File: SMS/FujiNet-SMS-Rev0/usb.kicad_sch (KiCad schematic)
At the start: 15 parts, among them J4 USB-C, U10 CP2102N-A02-GQFN28, U11 UMH3N

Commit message: SMS Rev0 v2: co-designed floorplan, region sheets, E9 pull-downs, frozen refs and nets
Floorplan study (docs/floorplan-study.md): the SMS edge is the JEDEC
32-pin memory pinout unrolled, so SRAM0 standing upright in the ROM spot
takes A0-A12 / D0-D7 / GND with no crossing.  gen_pcb.sram0_fanin draws
that fan-in locked (funnel, two corner wraps, B-finger jog vias, escape
vias for CE# and OE#).  Four candidates scored and trial-routed in
parallel; P3 (RP2354B straight north of SRAM0, SRAM1 west, glue east over
the strobes) routes best (45 unrouted after 4 passes vs 50 for the first
layout) and reads straight across on the schematic page.

- placement.py: candidates as blocks; the RP2354B + ring as a rigid macro
  (turns as a whole, dvdd_island turns with it); per-variant In4 +5V
  island polygon; label area for the shell
- design.py: sheets are board regions (cart-bus, rp-core, fujinet, usb,
  power); the RP2354B as a two-unit symbol (GPIO on cart-bus, core on
  rp-core); resistor packs one unit per resistor; RP2350-E9 4.7k
  pull-downs on GAME/LOAD/RAM_WE/MBOX/SA19 (check_nets asserts <= 8.2k);
  bring-up pads (CE, OE, WE, PWR_OK, rails, DVDD)
- geographic references (tools/annotate.py -> tools/refs.lock); net names
  frozen in tools/nets.lock (gen_sch fails if a redraw changes one)
- sch_draft.py: an every-pin-labelled draft of the final hierarchy so the
  board is built while the sheets are drawn; sch_draw lint for wired
  sheets (one piece per net, no 4-way junctions, wires clear of text,
  crossing count); sch_place.py mirror check
- check_parts_inside: footprint keep-outs (the S3 antenna bars parts)
- shell: RESET plunger redesigned (captive flange under the guide, stem
  on the TS-1187A actuator, travel asserts, interference part)

ERC 0, parity 126/126, check_nets 442/442, check_glue 8192/8192.
Board placed, not routed yet.

Co-Authored-By: Claude Opus 5.5 <noreply@anthropic.com>
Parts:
- removed C34: 1uF, FujiNet-SMS:C_0603_1608Metric, symbol Device:C
- removed C35, C36: 100nF, FujiNet-SMS:C_0603_1608Metric, symbol Device:C
- removed C37: 4.7uF, FujiNet-SMS:C_0603_1608Metric, symbol Device:C
- removed D5, D6: ESD5Z5.0T1G, FujiNet-SMS:D_SOD-523, symbol Diode:ESD5Zxx
- removed J4: USB-C, FujiNet-SMS:USB_C_Receptacle_HRO_TYPE-C-31-M-12, symbol Connector:USB_C_Receptacle_USB2.0_16P
- removed R17, R18: 5.1k, FujiNet-SMS:R_0603_1608Metric, symbol Device:R
- removed R19: 22k, FujiNet-SMS:R_0603_1608Metric, symbol Device:R
- removed R20: 47k, FujiNet-SMS:R_0603_1608Metric, symbol Device:R
- removed R21: 10k, FujiNet-SMS:R_0603_1608Metric, symbol Device:R
- removed U10: CP2102N-A02-GQFN28, FujiNet-SMS:QFN-28-1EP_5x5mm_P0.5mm_EP3.35x3.35mm, symbol Interface_USB:CP2102N-Axx-xQFN28
- removed U11: UMH3N, FujiNet-SMS:SOT-363_SC-70-6, symbol Transistor_BJT:UMH3N
- added C13, C5: 100nF, FujiNet-SMS:C_0603_1608Metric, symbol Device:C
- added C14: 4.7uF, FujiNet-SMS:C_0603_1608Metric, symbol Device:C
- added C4: 1uF, FujiNet-SMS:C_0603_1608Metric, symbol Device:C
- added D2, D3: ESD5Z5.0T1G, FujiNet-SMS:D_SOD-523, symbol Diode:ESD5Zxx
- added J2: USB-C, FujiNet-SMS:USB_C_Receptacle_HRO_TYPE-C-31-M-12, symbol Connector:USB_C_Receptacle_USB2.0_16P
- added R1, R2: 5.1k, FujiNet-SMS:R_0603_1608Metric, symbol Device:R
- added R12: 22k, FujiNet-SMS:R_0603_1608Metric, symbol Device:R
- added R13: 47k, FujiNet-SMS:R_0603_1608Metric, symbol Device:R
- added R9: 10k, FujiNet-SMS:R_0603_1608Metric, symbol Device:R
- added U2: CP2102N-A02-GQFN28, FujiNet-SMS:QFN-28-1EP_5x5mm_P0.5mm_EP3.35x3.35mm, symbol Interface_USB:CP2102N-Axx-xQFN28
- added U3: UMH3N, FujiNet-SMS:SOT-363_SC-70-6, symbol Transistor_BJT:UMH3N
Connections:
- net +3V3: now also C13.1, C14.1, R9.1, U2.6 (VDD), U2.7 (VREGIN)
- net CC1: now also J2.A5 (CC1), R1.1
- net CC2: now also J2.B5 (CC2), R2.1
- net CP_RST: now also R9.2, U2.9 (~{RST})
- net GND: now also C13.2, C14.2, C4.2, C5.2, D2.2 (A), D3.2 (A), J2.A1 (GND), J2.A12 (GND), J2.B1 (GND), J2.B12 (GND), J2.SH (SHIELD), R1.2, R13.2, R2.2, U2.23 (~{CTS}), U2.29 (GND), U2.3 (GND)
- net S3_EN: now also U3.6 (C1)
- net S3_IO0: now also U3.3 (C2)
- net S3_RXD: now also U2.26 (TXD)
- net S3_TXD: now also U2.25 (RXD)
- net UART_DTR: now also U2.28 (~{DTR}), U3.2 (B1), U3.4 (E2)
- net UART_RTS: now also U2.24 (~{RTS}), U3.1 (E1), U3.5 (B2)
- net UBRG_DM: now also D4.1 (K), J2.A7 (D-), J2.B7 (D-), U2.5 (D-)
- net UBRG_DP: now also D3.1 (K), J2.A6 (D+), J2.B6 (D+), U2.4 (D+); no longer D4.1 (K)
- net VBUS: now also C4.1, C5.1, D2.1 (K), J2.A4 (VBUS), J2.A9 (VBUS), J2.B4 (VBUS), J2.B9 (VBUS), R12.1
- net VBUS_SNS: now also R12.2, R13.1, U2.8 (VBUS)
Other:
- title: FujiNet SMS Rev0 - USB-C, CP2102N bridge -> FujiNet SMS Rev0 - USB-C and the CP2102N bridge

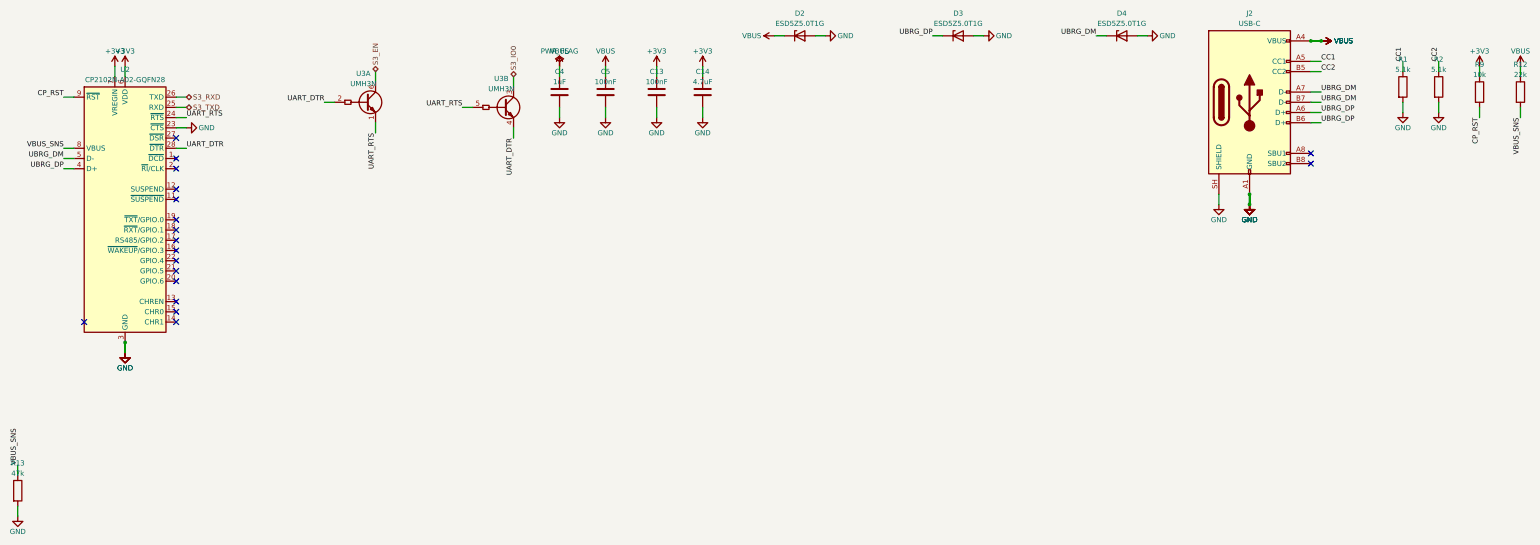
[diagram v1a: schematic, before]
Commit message: SMS Rev0 v2: redraw every sheet to mirror the board
Each sheet is now hand-placed in tools/sch_layout.py from where its parts
sit on the board, turned so the edge fingers face left (south -> left,
north -> right, west -> top, east -> bottom), and every connection on a
sheet is a wire:

- rp-core: the RP2354B core unit with its decoupling ring at the pins, the
  regulator corner, the crystal, SWD, RUN / BOOTSEL and the RESET diode
  (planar).
- fujinet: a functional ESP32-S3 symbol, EN / BOOT, the WS2812, and the
  microSD's SPI lines stepping into the socket with the pull-ups between
  them (planar).
- usb: a functional USB-C symbol, the CP2102N mirrored to face the
  receptacle, and the auto-program pair.  This page has one crossing, which
  cannot be avoided: RTS and DTR sit side by side on the bridge and each
  feeds the base of one transistor and the emitter of the other.
- power: the CONS_5V / VBUS OR on one +5V line, the LDO above it, the buck
  below it, and the rail PWR_FLAGs grouped together (planar).
- root: the board outline at 2:1, turned the same way, with each sheet's
  block at its region and the nine signals between sheets wired without a
  crossing; notes cover the stack-up and the firmware contract.

Gates: gen_sch.py checks the mirror (Kendall tau >= 0.85 per axis for the
major parts, multi-unit packages counted at the centre of their units,
parts within 5 mm on the board counted as level; every sheet is at
1.00 / 1.00) and a crossing budget per sheet (cart-bus 75, usb 1,
others 0).  ERC is 0 at all severities, netlist parity holds, the net
names equal tools/nets.lock, check_nets passes 442/442, check_glue
8192/8192, and edge_orientation passes.

Co-Authored-By: Claude Opus 5.5 <noreply@anthropic.com>
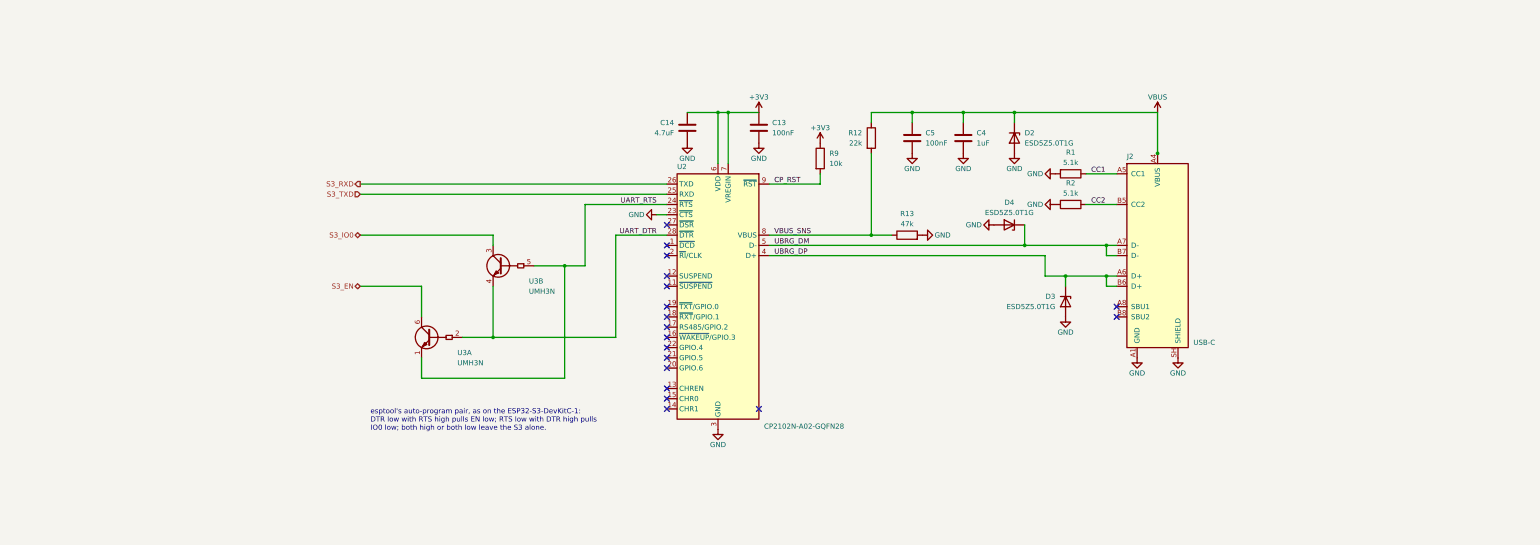
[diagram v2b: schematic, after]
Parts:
- J2: symbol Connector:USB_C_Receptacle_USB2.0_16P -> FujiNet-SMS:USB_C_USB2.0_16P_Fn
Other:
- note added: "esptool's auto-program pair, as on the ESP32-S3-DevKitC-1: DTR low with RTS high pulls EN low; RTS low with DTR high pulls IO0 low; both high or both low leave the S3 alone."
- moved on the sheet: C13, C14, C4, C5, D2, D3, D4, R1, R12, R13, R2, R9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
